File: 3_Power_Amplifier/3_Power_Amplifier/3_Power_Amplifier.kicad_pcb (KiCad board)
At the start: 2 copper layers, 100 x 100 mm, 24 parts, among them P1 SIGNAL_INPUT, P10 SWITCHED_POWER_INV, P11 SIGNAL_INPUT, P12 SWITCHED_POWER_INV, P2 SWITCHED_POWER_INV, P3 ISLETA, P4 ISLETA, P5 ISLETA, P6 ISLETA, P7 SIGNAL_INPUT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

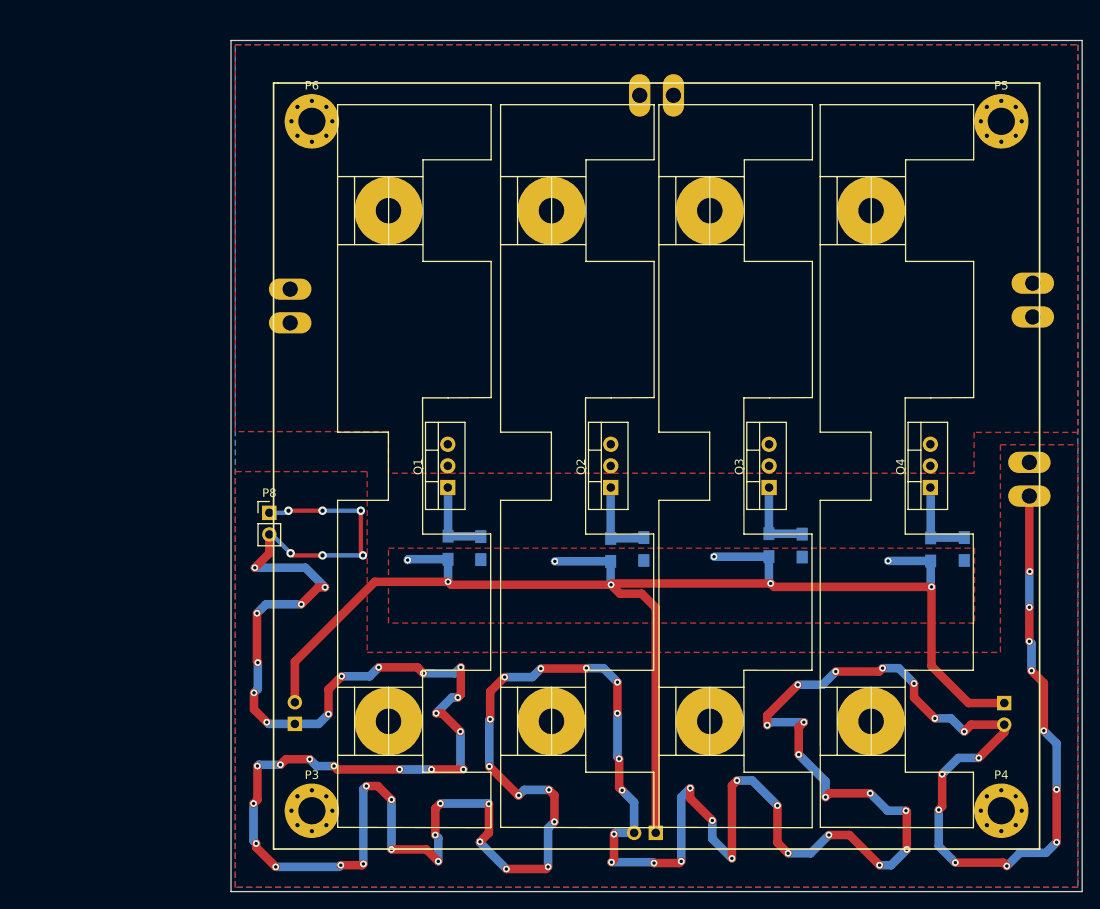
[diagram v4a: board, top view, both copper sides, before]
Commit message: AMPLIFICADOR DE POTENCIA_2 PCB_V5
LLENADO DE VIAS Y PLANOS PARA SOLDAR
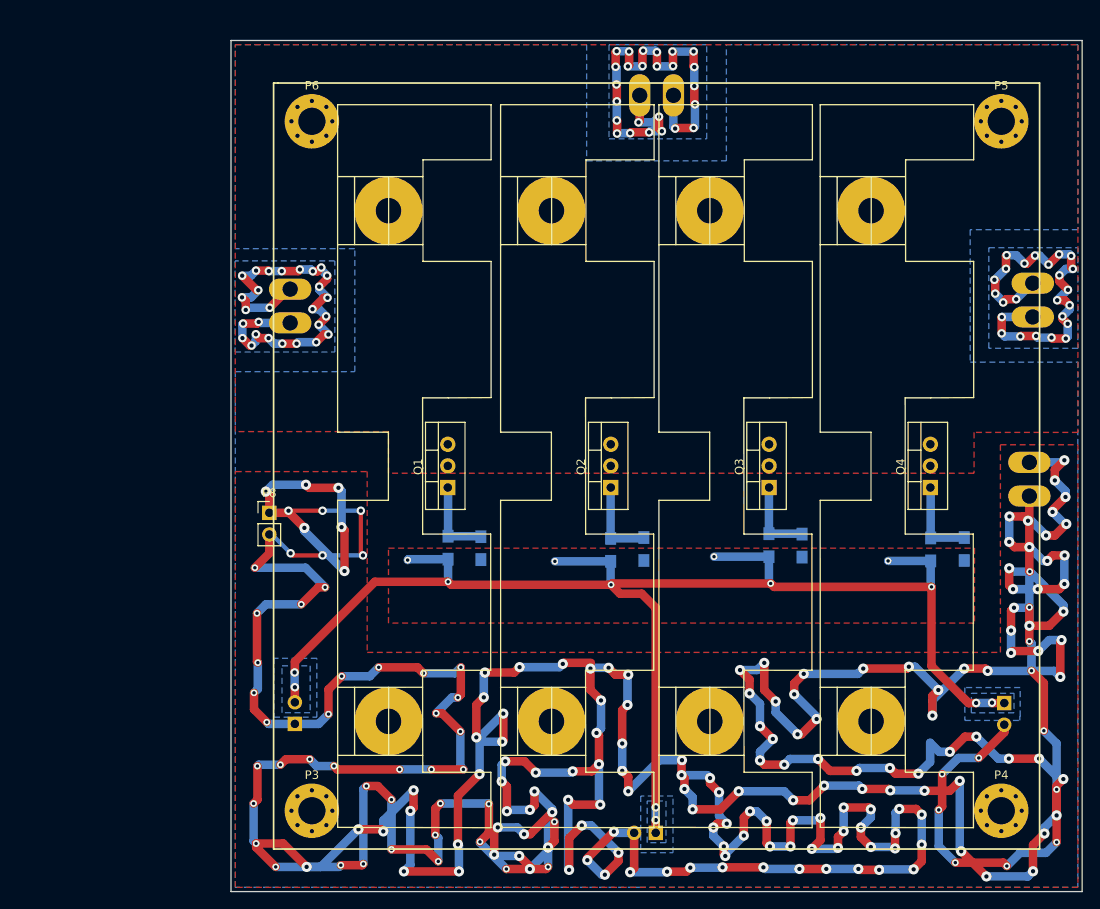
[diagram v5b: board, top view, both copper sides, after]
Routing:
- net /GND: track 485.8 -> 926.6 mm, vias 92 -> 212
- net /SWITCHED_POWER: track 0.00 -> 156.3 mm, vias 0 -> 76
- net /DDS: track 170.8 -> 171.8 mm, vias 8 -> 14
- added copper zone on B.Cu, net /DDS
- added copper zone on B.Cu, net /SWITCHED_POWER

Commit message: AMPLIFICADOR DE POTENCIA_2 PCB_V6
NUEVAS HUELLAS DEL COOLER
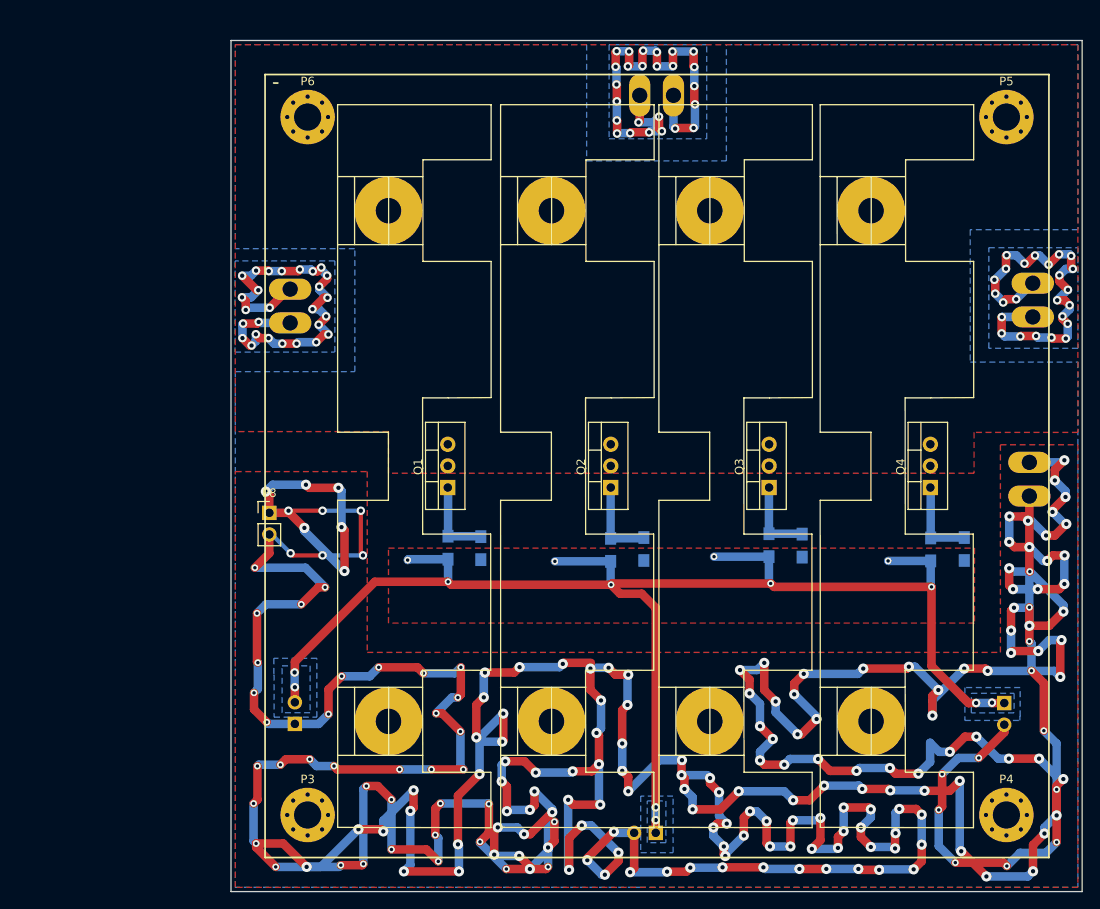
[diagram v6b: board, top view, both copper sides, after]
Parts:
- moved P4 0.78 mm to (169.6, 136.5)
- moved P5 0.78 mm to (169.6, 54.5)
- moved P3 0.71 mm to (87.5, 136.5)
- moved P6 0.71 mm to (87.5, 54.5)
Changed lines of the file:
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@@
     (links 41)
     (no_connects 4)
-    (area 78.424999 45.424999 178.623961 145.825001)
+    (area 78.424999 45.424999 178.575001 145.575001)
     (thickness 1.6)
     (drawings 23)
@@
   )
   (module Mounting_Holes:MountingHole_3.2mm_M3_Pad_Via (layer F.Cu)
-    (at 88 136)
+    (at 87.5 136.5)
     (descr "Mounting Hole 3.2mm, M3")
     (tags "mounting hole 3.2mm m3")
@@
   )
   (module Mounting_Holes:MountingHole_3.2mm_M3_Pad_Via (layer F.Cu)
-    (at 169 136)
+    (at 169.6 136.5)
     (descr "Mounting Hole 3.2mm, M3")
     (tags "mounting hole 3.2mm m3")
@@
   )
   (module Mounting_Holes:MountingHole_3.2mm_M3_Pad_Via (layer F.Cu)
-    (at 169 55)
+    (at 169.6 54.5)
     (descr "Mounting Hole 3.2mm, M3")
     (tags "mounting hole 3.2mm m3")
@@
   )
   (module Mounting_Holes:MountingHole_3.2mm_M3_Pad_Via (layer F.Cu)
-    (at 88 55)
+    (at 87.5 54.5)
     (descr "Mounting Hole 3.2mm, M3")
     (tags "mounting hole 3.2mm m3")
@@
     )
   )
+  (gr_line (start 82.5 49.5) (end 82.5 141.5) (angle 90) (layer F.SilkS) (width 0.2))
+  (gr_line (start 174.6 49.5) (end 82.5 49.5) (angle 90) (layer F.SilkS) (width 0.2))
+  (gr_line (start 174.6 141.5) (end 174.6 49.5) (angle 90) (layer F.SilkS) (width 0.2))
+  (gr_line (start 82.5 141.5) (end 174.6 141.5) (angle 90) (layer F.SilkS) (width 0.2))
   (gr_text SWITCHED_POWER (at 166 75.25 90) (layer B.SilkS)
     (effects (font (size 1.5 1.5) (thickness 0.3)) (justify mirror))
@@
     (effects (font (size 1.5 1.5) (thickness 0.3)) (justify mirror))
   )
-  (gr_line (start 83.5 50.5) (end 83.5 140.5) (angle 90) (layer F.SilkS) (width 0.2))
   (gr_line (start 84 50.5) (end 83.5 50.5) (angle 90) (layer F.SilkS) (width 0.2))
-  (gr_line (start 173.5 50.5) (end 84 50.5) (angle 90) (layer F.SilkS) (width 0.2))
-  (gr_line (start 173.5 140.5) (end 173.5 50.5) (angle 90) (layer F.SilkS) (width 0.2))
-  (gr_line (start 83.5 140.5) (end 173.5 140.5) (angle 90) (layer F.SilkS) (width 0.2))
   (gr_text DDS (at 127.4 135.7) (layer B.SilkS)
     (effects (font (size 1.5 1.5) (thickness 0.3)) (justify mirror))

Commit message: GENERADOR_V6
ESQUEMATICO LISTO PERO POR REVISAR
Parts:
- P1: value SIGNAL_INPUT -> SIGNAL_INPUT_SMA; footprint libreria_Power_Amplifier_huellas:REDISEÑADO_INV_Pin_Header_Pitch2.54mm -> libreria_Power_Amplifier_huellas:INV_SMA_THT_Jack_Straight
- P8: value TIERRAA -> TIERRA; footprint Pin_Headers:Pin_Header_Straight_1x02_Pitch2.54mm -> libreria_Power_Amplifier_huellas:INV_Socket_MOLEX-2-pines
- moved P8 2.19 mm to (84.6, 102.5), turned to 90 degrees
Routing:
- net (no net): track 0.00 -> 18.5 mm
- net /GND: track 926.6 -> 935.6 mm, vias 212 -> 210

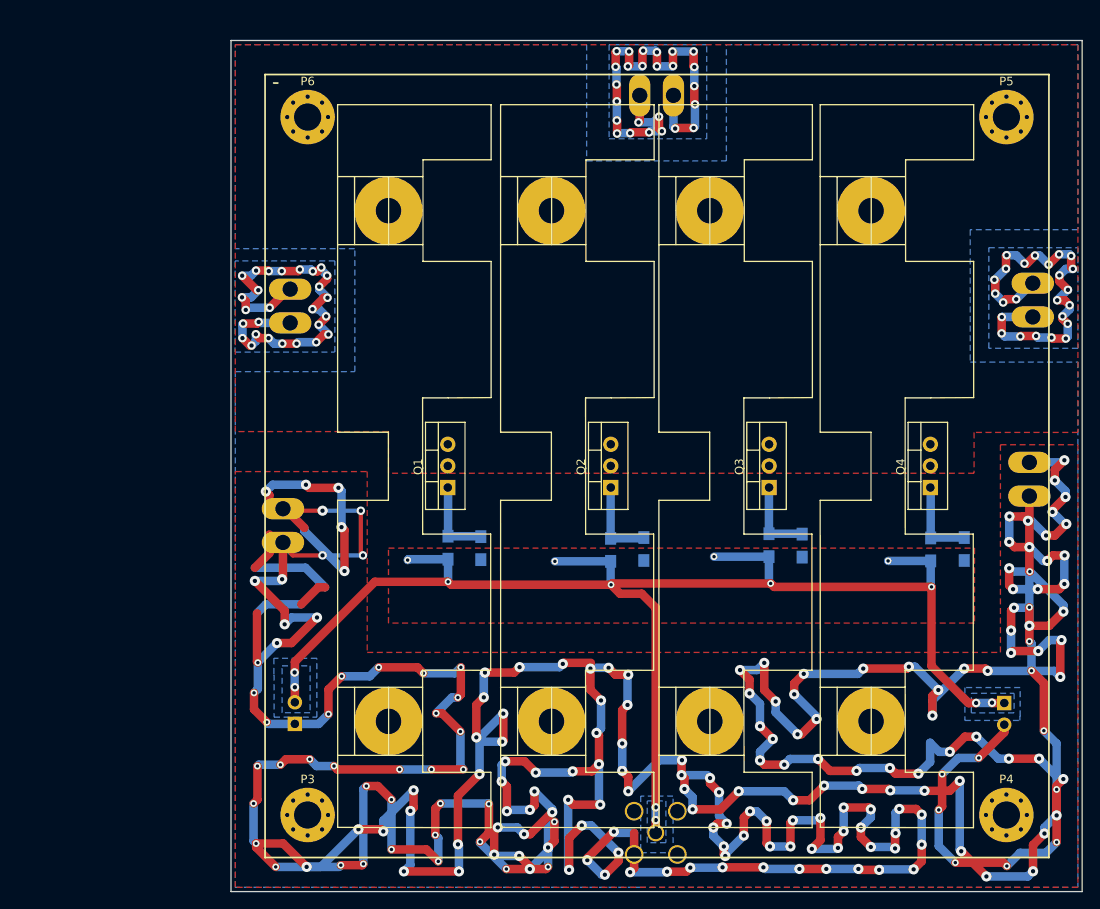
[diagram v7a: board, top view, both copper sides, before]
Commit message: POWER_AMPLIFIER_FINISH
ULTIMOS CAMBIOS DE PLANOS EN PLACA DE MOSFET
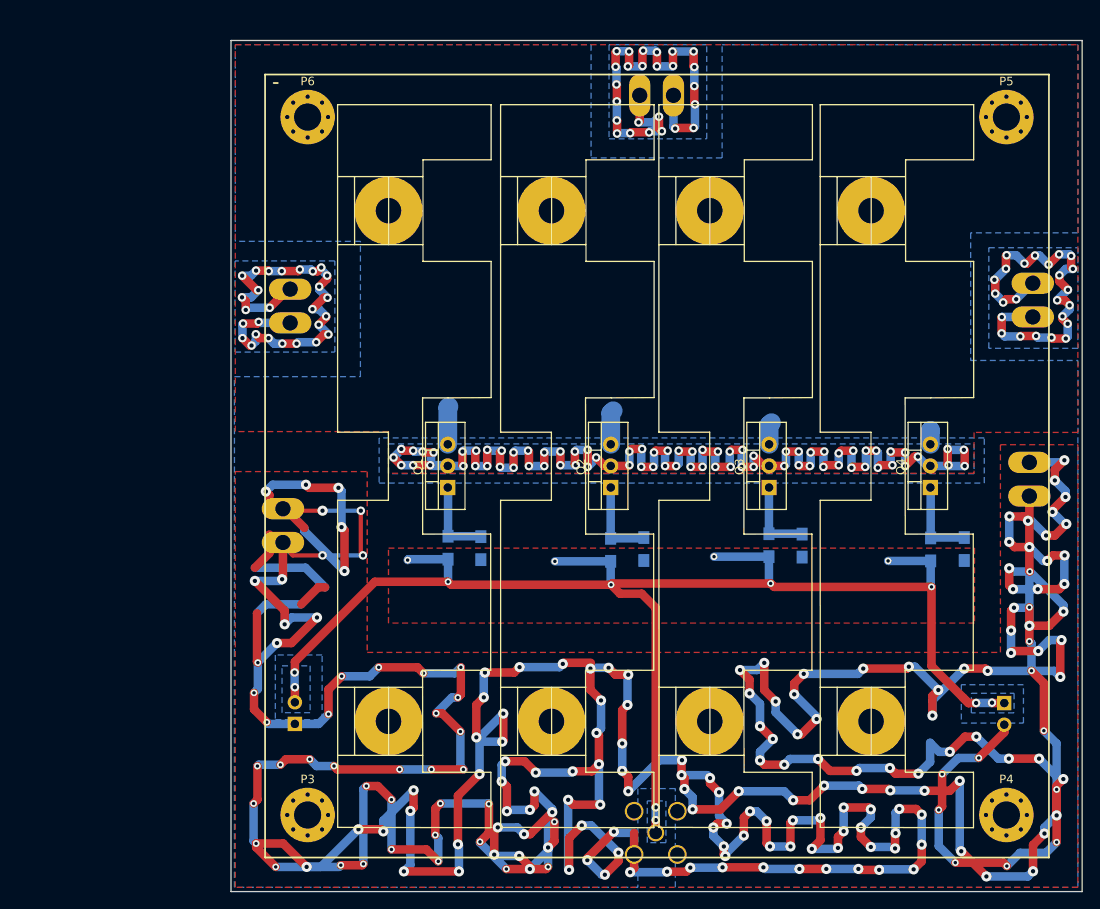
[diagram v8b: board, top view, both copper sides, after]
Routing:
- net /SWITCHED_POWER: track 156.3 -> 299.1 mm, vias 76 -> 152
- net /GND: track 935.6 -> 948.5 mm
